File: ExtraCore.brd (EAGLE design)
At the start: 19.8 x 22.4 mm, 19 parts, among them Y1 RESONATORSMD

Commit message: migrated to 28vqfn
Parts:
- removed ATMEGAXX8: ATMEGA168, SparkFun:TQFP32-08
- added UC1: ATMEGAXX8, Dustin:28VQFN
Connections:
- new net N$7: UC1.18, UC1.4, UC1.PAD
- net A0: now also UC1.19; no longer ATMEGAXX8.23
- net A1: now also UC1.20; no longer ATMEGAXX8.24
- net A2: now also UC1.21; no longer ATMEGAXX8.25
- net A3: now also UC1.22; no longer ATMEGAXX8.26
- net A4: now also UC1.23; no longer ATMEGAXX8.27
- net A5: now also UC1.24; no longer ATMEGAXX8.28
- net A6: no longer ATMEGAXX8.19
- net A7: no longer ATMEGAXX8.22
- net AREF: now also UC1.17; no longer ATMEGAXX8.20
- net AVCC: now also UC1.16; no longer ATMEGAXX8.18
- net D10: now also UC1.12; no longer ATMEGAXX8.14
- net D2: now also UC1.28; no longer ATMEGAXX8.32
- net D3: now also UC1.1; no longer ATMEGAXX8.1
- net D4: now also UC1.2; no longer ATMEGAXX8.2
- net D5: now also UC1.7; no longer ATMEGAXX8.9
- net D6: now also UC1.8; no longer ATMEGAXX8.10
- net D7: now also UC1.9; no longer ATMEGAXX8.11
- net D8: now also UC1.10; no longer ATMEGAXX8.12
- net D9: now also UC1.11; no longer ATMEGAXX8.13
- net GND: no longer ATMEGAXX8.21, ATMEGAXX8.3, ATMEGAXX8.5
- net MISO: now also UC1.14; no longer ATMEGAXX8.16
- net MOSI: now also UC1.13; no longer ATMEGAXX8.15
- net N$3: now also UC1.5; no longer ATMEGAXX8.7
- net N$4: now also UC1.6; no longer ATMEGAXX8.8
- net RESET: now also UC1.25; no longer ATMEGAXX8.29
- net RX: now also UC1.26; no longer ATMEGAXX8.30
- net SCK: now also UC1.15; no longer ATMEGAXX8.17
- net TX: now also UC1.27; no longer ATMEGAXX8.31
- net VCC: now also UC1.3; no longer ATMEGAXX8.4, ATMEGAXX8.6

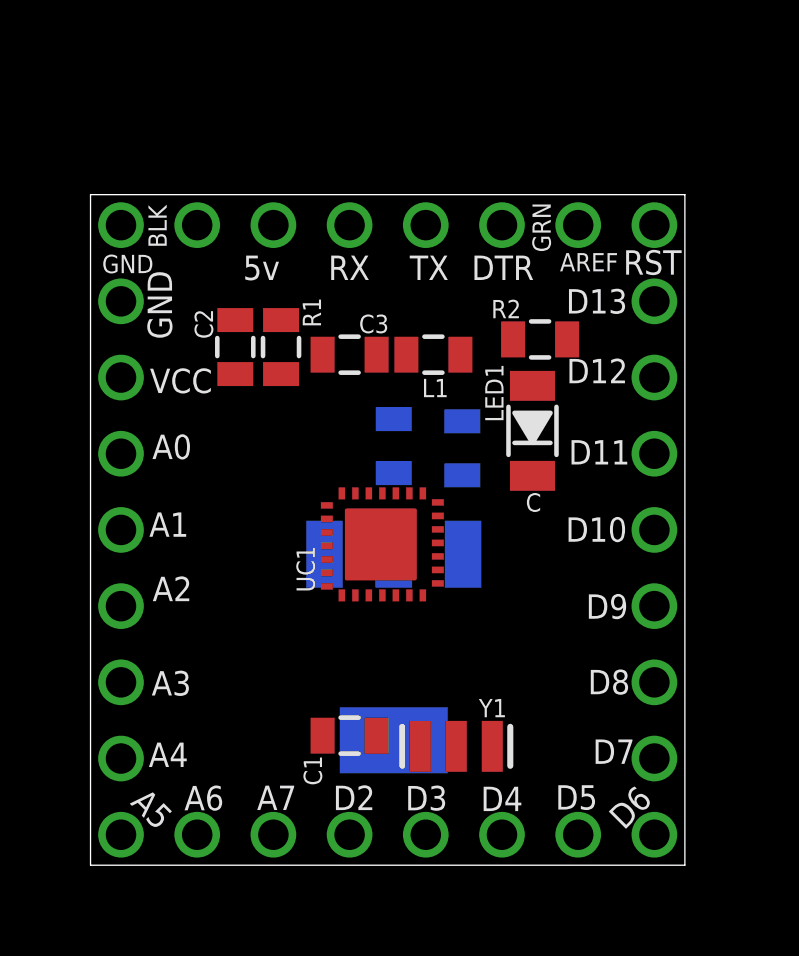
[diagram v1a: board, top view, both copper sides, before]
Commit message: changed all headers to 2mm
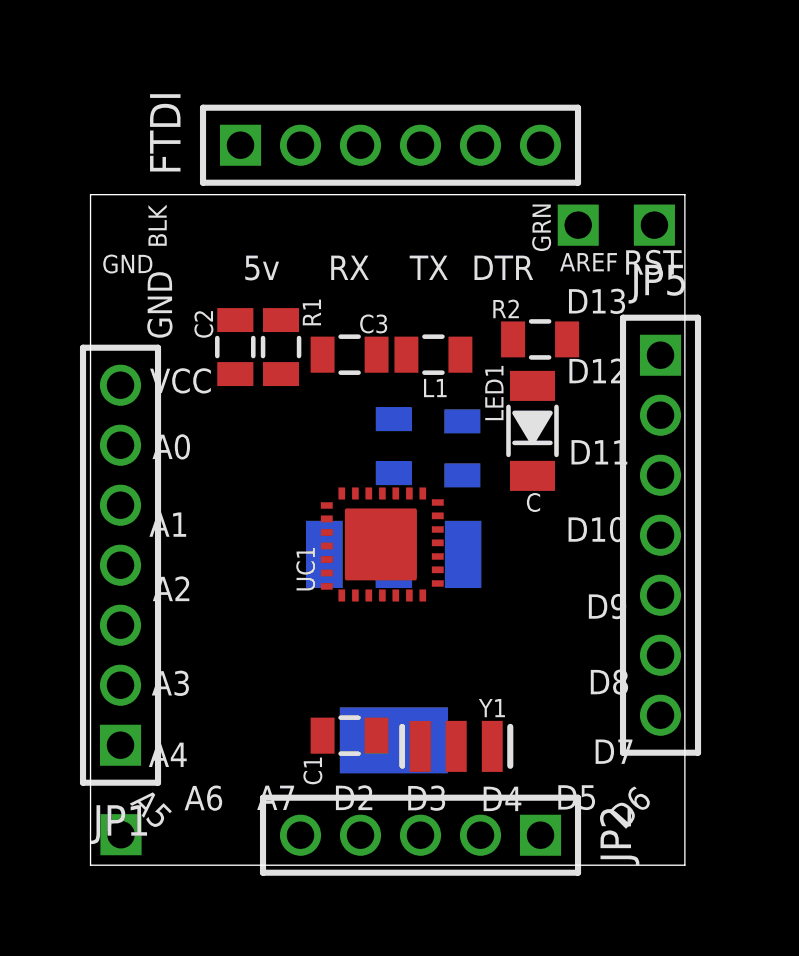
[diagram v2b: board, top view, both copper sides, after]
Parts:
- removed JP3: Analog1 & Digital0, SparkFun:1X07
- removed JP4: Digital1, SparkFun:1X07
- added FTDI: (no value), pinhead:1X06M
- added JP5: (no value), pinhead:1X07M
- A5, AREF, RESET: value M01PTH -> (none); device SparkFun:1X01 -> pinhead:1X01M
- JP1: value FTDI Basic -> (none); device SparkFun:1X06 -> pinhead:1X07M
- JP2: value Analog0 -> (none); device SparkFun:1X07 -> pinhead:1X05M
- moved JP1 11.3 mm to (1.00, 10.0), turned to 90 degrees
- moved JP2 10.3 mm to (11.0, 1.00), turned to 180 degrees
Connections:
- removed net A6: JP3.7
- removed net A7: JP3.6
- net A0: now also JP1.5; no longer JP2.5
- net A1: now also JP1.4; no longer JP2.4
- net A2: now also JP1.3; no longer JP2.3
- net A3: now also JP1.2; no longer JP2.2
- net A4: now also JP1.1; no longer JP2.1
- net D10: now also JP5.4; no longer JP4.4
- net D2: now also JP2.5; no longer JP3.5
- net D3: now also JP2.4; no longer JP3.4
- net D4: now also JP2.3; no longer JP3.3
- net D5: now also JP2.2; no longer JP3.2
- net D6: now also JP2.1; no longer JP3.1
- net D7: now also JP5.7; no longer JP4.7
- net D8: now also JP5.6; no longer JP4.6
- net D9: now also JP5.5; no longer JP4.5
- net DTR: now also FTDI.6; no longer JP1.6
- net GND: now also FTDI.1, FTDI.2; no longer JP1.1, JP1.2
- net MISO: now also JP5.2; no longer JP4.2
- net MOSI: now also JP5.3; no longer JP4.3
- net RAW: now also JP1.7; no longer JP2.7
- net RX: now also FTDI.4; no longer JP1.4
- net SCK: now also JP5.1; no longer JP4.1
- net TX: now also FTDI.5; no longer JP1.5
- net VCC: now also FTDI.3, JP1.6; no longer JP1.3, JP2.6

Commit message: moved stuff around. It's close to routable I think.
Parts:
- removed LED1: GREEN, ExtraCore:LED1206
- added LED2: (no value), SparkFun-LED:LED-0603
- moved C2 9.06 mm to (13.9, 16.9)
- moved A5 6.38 mm to (7.23, 2.46)
- moved FTDI 5.15 mm to (8.87, 19.0)
- moved RG1 5.00 mm to (13.1, 11.3)
- moved C1 4.30 mm to (12.9, 4.98)
- moved R2 3.40 mm to (15.2, 14.1), turned to 90 degrees
- moved C4 3.03 mm to (14.1, 16.4), turned to 0 degrees
- moved RESET 2.97 mm to (17.2, 18.8)
- moved JP1 2.86 mm to (3.80, 10.6)
- moved Y1 2.69 mm to (12.1, 6.65)
- moved L1 2.51 mm to (12.0, 14.6), turned to 90 degrees
- moved AREF 2.50 mm to (15.7, 18.9)
- moved JP2 2.41 mm to (12.9, 2.44)
- moved C3 2.37 mm to (8.61, 14.7)
- moved R1 2.26 mm to (8.60, 17.5), turned to 180 degrees
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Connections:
- net GND: now also LED2.C; no longer LED1.K
- net N$6: now also LED2.A; no longer LED1.A
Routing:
- net GND: track 0.00 -> 47.2 mm, vias 0 -> 4
- net VCC: track 0.00 -> 43.7 mm, vias 0 -> 2
- net RESET: track 0.00 -> 23.2 mm, vias 0 -> 2
- net AREF: track 0.00 -> 15.8 mm
- net RAW: track 0.00 -> 14.8 mm, vias 0 -> 2
- net TX: track 0.00 -> 13.8 mm, vias 0 -> 1
- net N$6: track 0.00 -> 13.4 mm, vias 0 -> 2
- net RX: track 0.00 -> 12.2 mm, vias 0 -> 1
- net D4: track 0.00 -> 10.8 mm, vias 0 -> 1
- net A4: track 0.00 -> 10.7 mm
- net D6: track 0.00 -> 8.91 mm
- net A3: track 0.00 -> 8.88 mm
- net D3: track 0.00 -> 8.65 mm, vias 0 -> 2
- net SCK: track 0.00 -> 8.16 mm
- net D2: track 0.00 -> 8.13 mm
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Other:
- board size 19.8 x 22.4 mm -> 15.3 x 18.6 mm

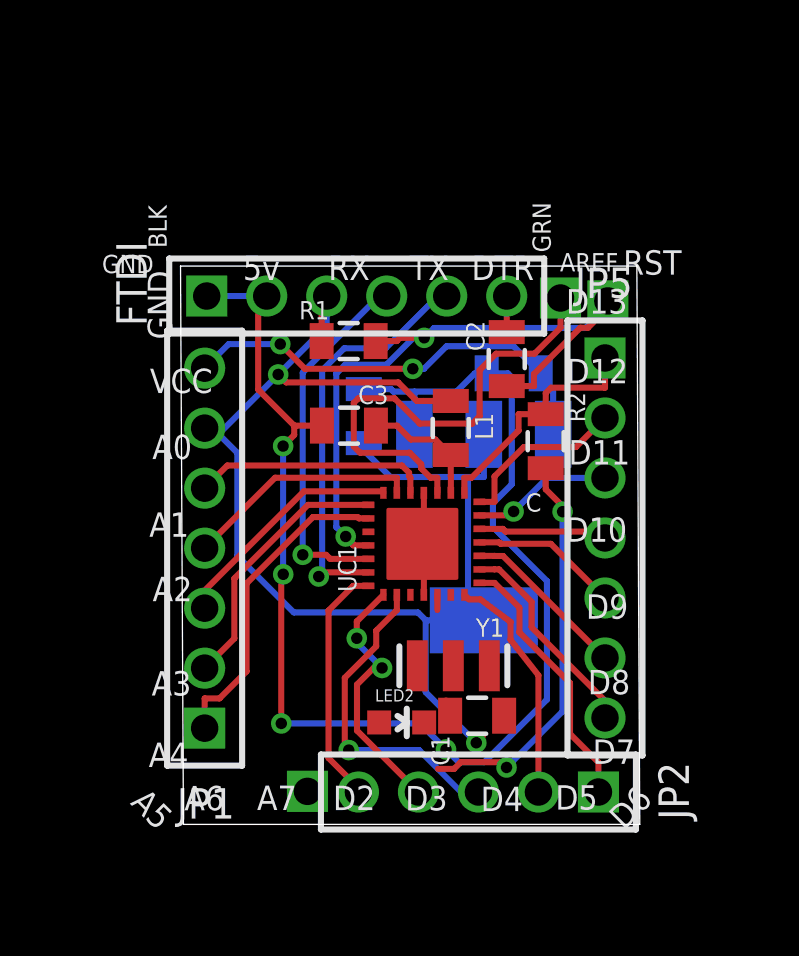
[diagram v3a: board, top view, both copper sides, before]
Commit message: moved headers into position and routed all traces
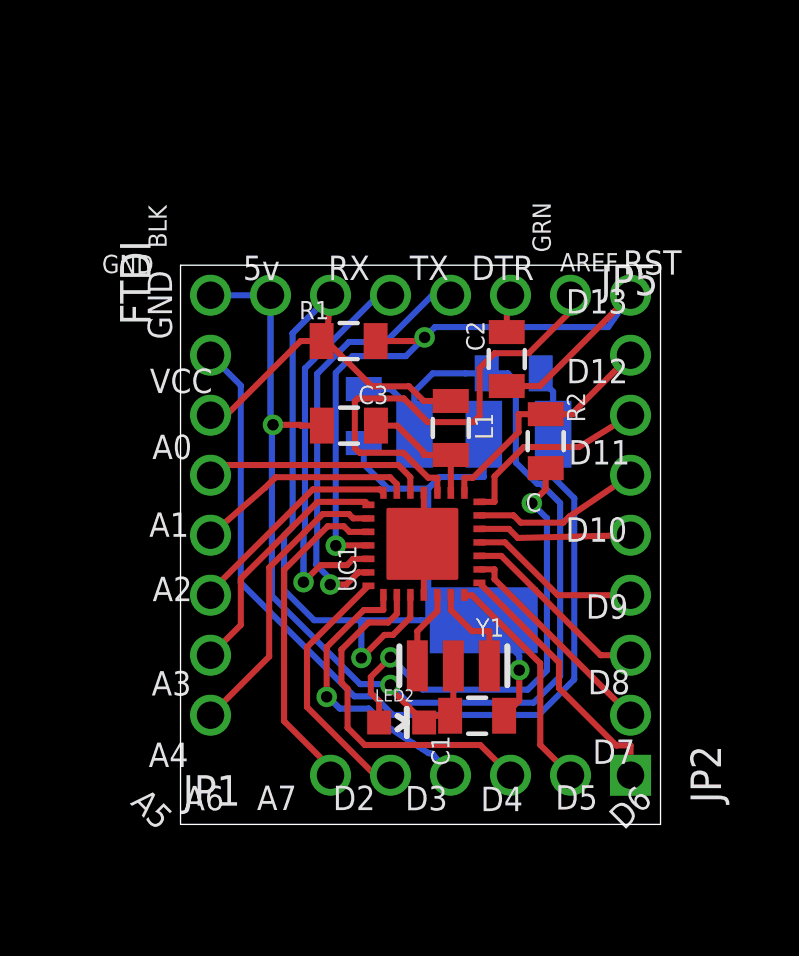
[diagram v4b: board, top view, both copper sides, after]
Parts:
- moved JP5 6.15 mm to (18.0, 17.0)
- moved JP1 5.57 mm to (4.00, 5.00)
- moved JP2 5.10 mm to (18.0, 3.00)
- moved FTDI 4.87 mm to (4.00, 19.0)
- moved A5 0.94 mm to (8.00, 3.00)
- moved RESET 0.78 mm to (18.0, 19.0)
- moved AREF 0.35 mm to (16.0, 19.0)
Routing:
- net RAW: track 14.8 -> 32.1 mm, vias 2 -> 0
- net A5: track 0.00 -> 10.9 mm
- net VCC: track 43.7 -> 48.0 mm
- net N$4: track 0.00 -> 3.23 mm
- net N$6: track 13.4 -> 15.6 mm
- net N$3: track 0.50 -> 2.64 mm
- net RESET: track 23.2 -> 24.9 mm
- net RX: track 12.2 -> 13.5 mm
- net D3: track 8.65 -> 9.69 mm, vias 2 -> 1
- net MOSI: track 4.70 -> 5.64 mm, vias 1 -> 0
- net D4: track 10.8 -> 11.7 mm, vias 1 -> 0
- net D10: track 4.31 -> 5.17 mm
- net A4: track 10.7 -> 9.84 mm
- net D9: track 4.96 -> 5.77 mm
- net D8: track 5.60 -> 6.41 mm
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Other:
- board size 15.3 x 18.6 mm -> 16 x 18.6 mm
